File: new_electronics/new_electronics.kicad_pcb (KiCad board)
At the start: 2 copper layers, 17 parts

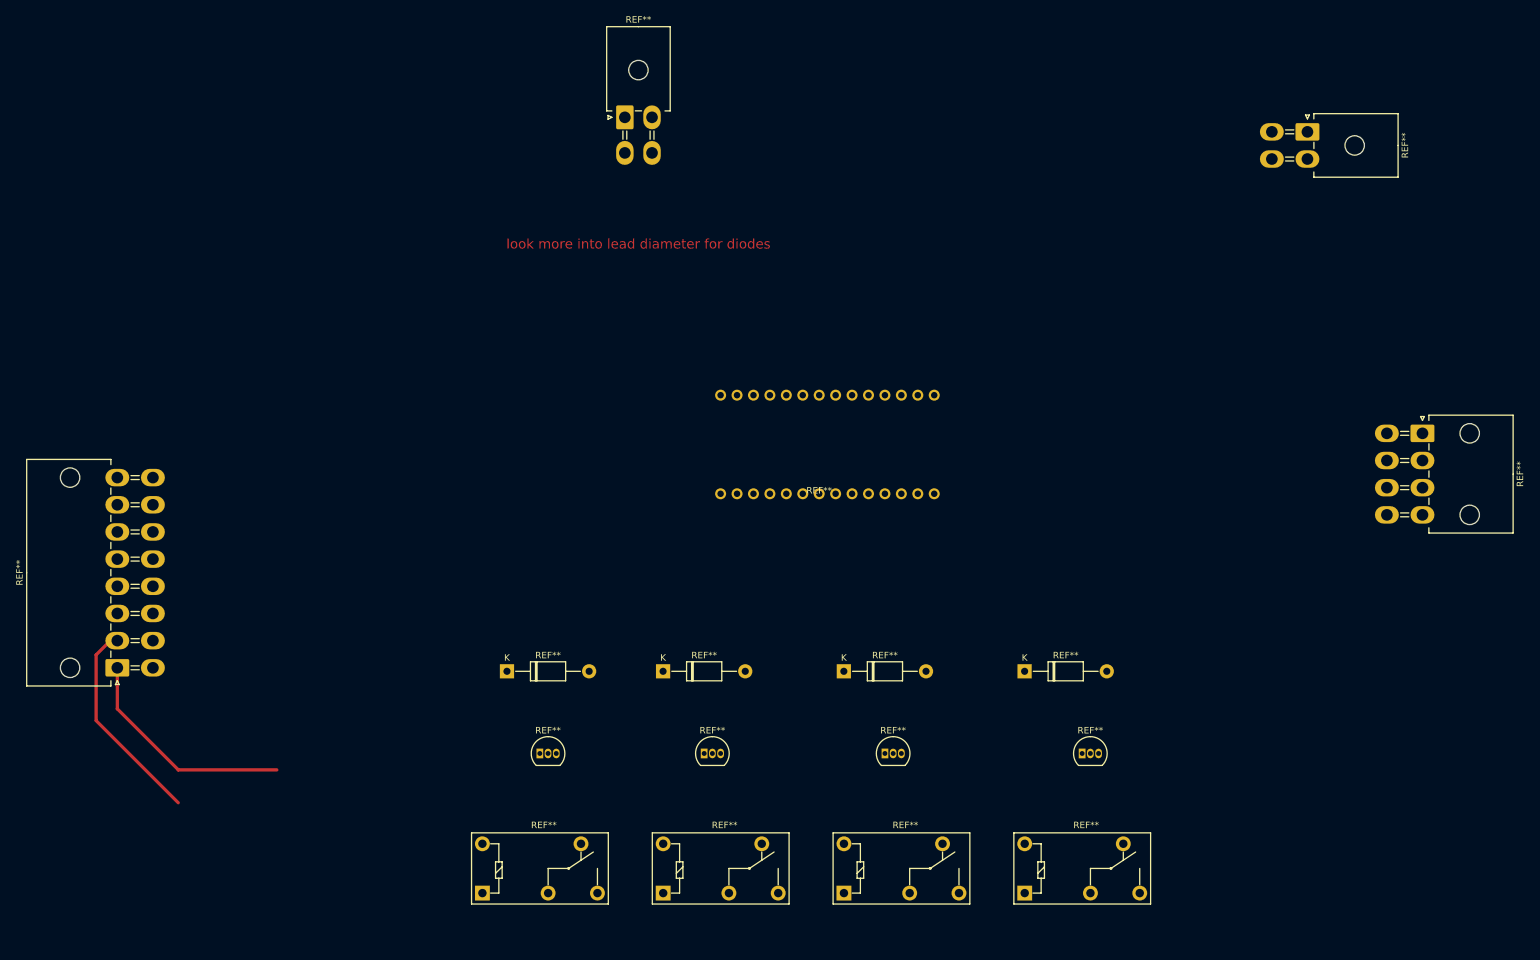
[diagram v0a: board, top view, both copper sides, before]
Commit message: some basic wiring for new pcb
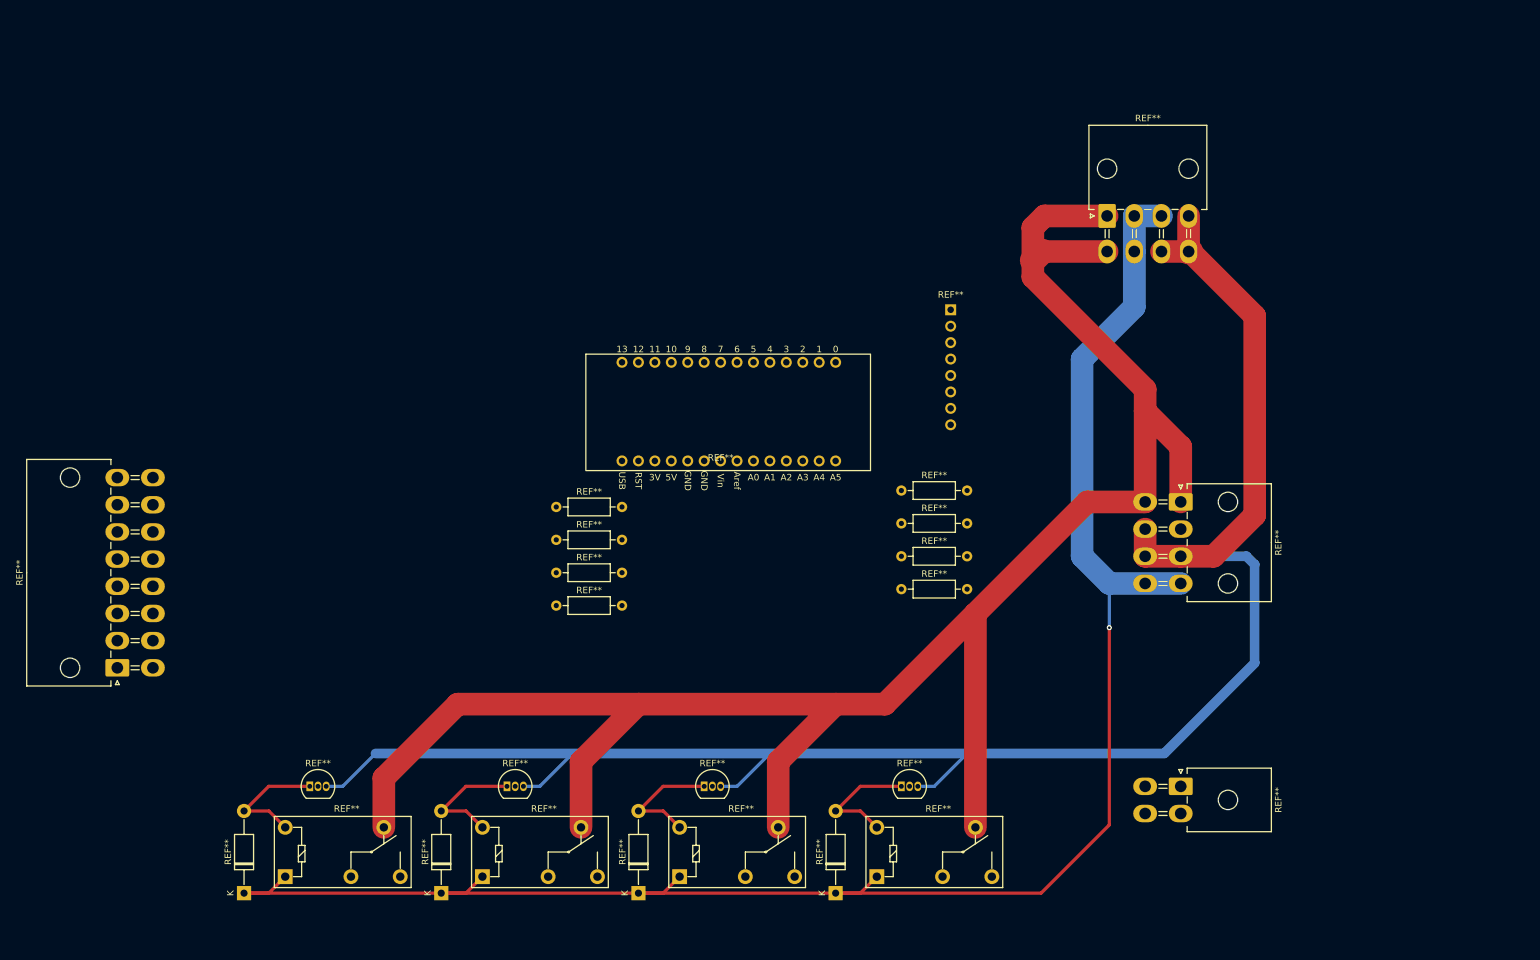
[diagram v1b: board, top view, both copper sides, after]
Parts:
- removed the REF** at (118.1, 119.4)
- removed the REF** at (146.1, 119.4)
- removed the REF** at (112.2, 33.8)
- removed the REF** at (174.0, 119.4)
- added REF**: R_Axial_DIN0207_L6.3mm_D2.5mm_P10.16mm_Horizontal, Resistor_THT:R_Axial_DIN0207_L6.3mm_D2.5mm_P10.16mm_Horizontal, F.Cu at (101.6, 104.1)
- added REF**: R_Axial_DIN0207_L6.3mm_D2.5mm_P10.16mm_Horizontal, Resistor_THT:R_Axial_DIN0207_L6.3mm_D2.5mm_P10.16mm_Horizontal, F.Cu at (101.6, 109.2)
- added REF**: R_Axial_DIN0207_L6.3mm_D2.5mm_P10.16mm_Horizontal, Resistor_THT:R_Axial_DIN0207_L6.3mm_D2.5mm_P10.16mm_Horizontal, F.Cu at (101.6, 94.0)
- added REF**: Molex_Mini-Fit_Jr_5569-08A2_2x04_P4.20mm_Horizontal, Connector_Molex:Molex_Mini-Fit_Jr_5569-08A2_2x04_P4.20mm_Horizontal, F.Cu at (186.7, 49.0)
- added REF**: D_DO-41_SOD81_P12.70mm_Horizontal, Diode_THT:D_DO-41_SOD81_P12.70mm_Horizontal, F.Cu at (114.3, 153.7)
- added REF**: R_Axial_DIN0207_L6.3mm_D2.5mm_P10.16mm_Horizontal, Resistor_THT:R_Axial_DIN0207_L6.3mm_D2.5mm_P10.16mm_Horizontal, F.Cu at (154.9, 101.6)
- added REF**: R_Axial_DIN0207_L6.3mm_D2.5mm_P10.16mm_Horizontal, Resistor_THT:R_Axial_DIN0207_L6.3mm_D2.5mm_P10.16mm_Horizontal, F.Cu at (154.9, 96.5)
- added REF**: D_DO-41_SOD81_P12.70mm_Horizontal, Diode_THT:D_DO-41_SOD81_P12.70mm_Horizontal, F.Cu at (144.8, 153.7)
- added REF**: mpu6050, custom_footprints:mpu6050, F.Cu at (162.6, 71.1)
- added REF**: R_Axial_DIN0207_L6.3mm_D2.5mm_P10.16mm_Horizontal, Resistor_THT:R_Axial_DIN0207_L6.3mm_D2.5mm_P10.16mm_Horizontal, F.Cu at (101.6, 99.1)
- added REF**: R_Axial_DIN0207_L6.3mm_D2.5mm_P10.16mm_Horizontal, Resistor_THT:R_Axial_DIN0207_L6.3mm_D2.5mm_P10.16mm_Horizontal, F.Cu at (154.9, 91.4)
- added REF**: D_DO-41_SOD81_P12.70mm_Horizontal, Diode_THT:D_DO-41_SOD81_P12.70mm_Horizontal, F.Cu at (83.8, 153.7)
- added REF**: R_Axial_DIN0207_L6.3mm_D2.5mm_P10.16mm_Horizontal, Resistor_THT:R_Axial_DIN0207_L6.3mm_D2.5mm_P10.16mm_Horizontal, F.Cu at (154.9, 106.7)
- moved REF** 103.0 mm to (198.1, 137.2)
- moved REF** 53.2 mm to (53.3, 153.7), turned to 90 degrees
- moved REF** 38.8 mm to (198.1, 93.2)
- moved REF** 35.9 mm to (63.5, 137.2)
- moved REF** 30.9 mm to (94.0, 137.2)
- moved REF** 30.6 mm to (59.7, 151.1)
- moved REF** 28.4 mm to (124.5, 137.2)
- moved REF** 28.4 mm to (154.9, 137.2)
- moved REF** 28.1 mm to (90.2, 151.1)
- moved REF** 25.5 mm to (120.7, 151.1)
- moved REF** 23.0 mm to (151.1, 151.1)
- moved REF** 16.1 mm to (127.0, 78.7)
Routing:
- net (no net): track 67.2 -> 957.9 mm, vias 0 -> 1
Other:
- board text removed: "look more into lead diameter for diodes"

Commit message: more new pcb work
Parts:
- removed the REF** at (154.9, 101.6)
- removed the REF** at (154.9, 96.5)
- removed the REF** at (154.9, 91.4)
- removed the REF** at (154.9, 106.7)
- added Controller Vin: TestPoint_Plated_Hole_D2.0mm, TestPoint:TestPoint_Plated_Hole_D2.0mm, F.Cu at (106.7, 87.6)
- added R1: R_Axial_DIN0207_L6.3mm_D2.5mm_P10.16mm_Horizontal, Resistor_THT:R_Axial_DIN0207_L6.3mm_D2.5mm_P10.16mm_Horizontal, F.Cu at (154.3, 78.1)
- added R2: R_Axial_DIN0207_L6.3mm_D2.5mm_P10.16mm_Horizontal, Resistor_THT:R_Axial_DIN0207_L6.3mm_D2.5mm_P10.16mm_Horizontal, F.Cu at (151.1, 78.1)
- added R3: R_Axial_DIN0207_L6.3mm_D2.5mm_P10.16mm_Horizontal, Resistor_THT:R_Axial_DIN0207_L6.3mm_D2.5mm_P10.16mm_Horizontal, F.Cu at (148.0, 78.1)
- added R4: R_Axial_DIN0207_L6.3mm_D2.5mm_P10.16mm_Horizontal, Resistor_THT:R_Axial_DIN0207_L6.3mm_D2.5mm_P10.16mm_Horizontal, F.Cu at (144.8, 78.1)
- added REF**: PinHeader_1x01_P2.54mm_Vertical, Connector_PinHeader_2.54mm:PinHeader_1x01_P2.54mm_Vertical, F.Cu at (125.7, 103.5)
- added REF**: PinHeader_1x03_P2.54mm_Vertical, Connector_PinHeader_2.54mm:PinHeader_1x03_P2.54mm_Vertical, F.Cu at (139.1, 105.4)
- 12-6V Converter: renamed from REF**
- Depth Sensor: renamed from REF**
- Main Connector: renamed from REF**
- Power I/O: renamed from REF**
- moved Main Connector 31.0 mm to (64.1, 125.1)
- moved U2 29.8 mm to (181.6, 94.0)
- moved 12-6V Converter 28.5 mm to (196.9, 75.7)
- moved R5 24.3 mm to (78.7, 85.7), turned to 90 degrees
- moved R6 22.8 mm to (81.9, 87.6), turned to 90 degrees
- moved R8 22.2 mm to (88.3, 91.4), turned to 90 degrees
- moved R7 22.0 mm to (85.1, 89.5), turned to 90 degrees
- moved Power I/O 15.9 mm to (198.1, 109.1)
- moved U1 15.4 mm to (136.5, 90.8)
- renumbered REF** to D1, REF** to D2, REF** to D3, REF** to D4, REF** to K1, REF** to K2, REF** to K3, REF** to K4, REF** to Q1, REF** to Q2, REF** to Q3, REF** to Q4, REF** to R5, REF** to R6, REF** to R7, REF** to R8, REF** to U1, REF** to U2
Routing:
- net (no net): track 957.9 -> 3714.9 mm, vias 1 -> 19
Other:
- board outline added: 165.1 x 101.6 mm

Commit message: 'finished' new pcb
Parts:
- removed Controller Vin: TestPoint_Plated_Hole_D2.0mm, TestPoint:TestPoint_Plated_Hole_D2.0mm
- removed REF**: PinHeader_1x01_P2.54mm_Vertical, Connector_PinHeader_2.54mm:PinHeader_1x01_P2.54mm_Vertical
- removed REF**: PinHeader_1x03_P2.54mm_Vertical, Connector_PinHeader_2.54mm:PinHeader_1x03_P2.54mm_Vertical
- added 8: PinHeader_1x01_P2.54mm_Vertical, Connector_PinHeader_2.54mm:PinHeader_1x01_P2.54mm_Vertical, F.Cu at (67.6, 88.9)
- added Controller Battery: Molex_Mini-Fit_Jr_5569-04A2_2x02_P4.20mm_Horizontal, Connector_Molex:Molex_Mini-Fit_Jr_5569-04A2_2x02_P4.20mm_Horizontal, F.Cu at (169.3, 75.7)
- added D5: LED_D5.0mm, LED_THT:LED_D5.0mm, F.Cu at (55.8, 68.1)
- added D6: LED_D5.0mm, LED_THT:LED_D5.0mm, F.Cu at (65.8, 68.1)
- added D7: LED_D5.0mm, LED_THT:LED_D5.0mm, F.Cu at (75.8, 68.1)
- added J1: PinHeader_1x03_P2.54mm_Vertical, Connector_PinHeader_2.54mm:PinHeader_1x03_P2.54mm_Vertical, F.Cu at (112.8, 107.4)
- added NC: PinHeader_1x01_P2.54mm_Vertical, Connector_PinHeader_2.54mm:PinHeader_1x01_P2.54mm_Vertical, F.Cu at (105.4, 138.5)
- added NC: PinHeader_1x01_P2.54mm_Vertical, Connector_PinHeader_2.54mm:PinHeader_1x01_P2.54mm_Vertical, F.Cu at (135.9, 138.5)
- added NC: PinHeader_1x01_P2.54mm_Vertical, Connector_PinHeader_2.54mm:PinHeader_1x01_P2.54mm_Vertical, F.Cu at (74.9, 138.5)
- added NC: PinHeader_1x01_P2.54mm_Vertical, Connector_PinHeader_2.54mm:PinHeader_1x01_P2.54mm_Vertical, F.Cu at (166.4, 138.5)
- added Q5: TO-92_Inline, Package_TO_SOT_THT:TO-92_Inline, F.Cu at (103.8, 66.0)
- added Q6: TO-92_Inline, Package_TO_SOT_THT:TO-92_Inline, F.Cu at (111.4, 66.0)
- added Q7: TO-92_Inline, Package_TO_SOT_THT:TO-92_Inline, F.Cu at (119.0, 66.0)
- added Q8: TO-92_Inline, Package_TO_SOT_THT:TO-92_Inline, F.Cu at (173.9, 123.7)
- added R10: R_Axial_DIN0207_L6.3mm_D2.5mm_P15.24mm_Horizontal, Resistor_THT:R_Axial_DIN0207_L6.3mm_D2.5mm_P15.24mm_Horizontal, F.Cu at (112.6, 73.4)
- added R11: R_Axial_DIN0207_L6.3mm_D2.5mm_P10.16mm_Horizontal, Resistor_THT:R_Axial_DIN0207_L6.3mm_D2.5mm_P10.16mm_Horizontal, F.Cu at (121.3, 80.8)
- added R12: R_Axial_DIN0207_L6.3mm_D2.5mm_P10.16mm_Horizontal, Resistor_THT:R_Axial_DIN0207_L6.3mm_D2.5mm_P10.16mm_Horizontal, F.Cu at (138.2, 66.5)
- added R13: R_Axial_DIN0207_L6.3mm_D2.5mm_P10.16mm_Horizontal, Resistor_THT:R_Axial_DIN0207_L6.3mm_D2.5mm_P10.16mm_Horizontal, F.Cu at (138.2, 69.6)
- added R14: R_Axial_DIN0207_L6.3mm_D2.5mm_P10.16mm_Horizontal, Resistor_THT:R_Axial_DIN0207_L6.3mm_D2.5mm_P10.16mm_Horizontal, F.Cu at (138.2, 72.6)
- added R15: R_Axial_DIN0207_L6.3mm_D2.5mm_P10.16mm_Horizontal, Resistor_THT:R_Axial_DIN0207_L6.3mm_D2.5mm_P10.16mm_Horizontal, F.Cu at (190.0, 127.8)
- added R16: R_Axial_DIN0207_L6.3mm_D2.5mm_P10.16mm_Horizontal, Resistor_THT:R_Axial_DIN0207_L6.3mm_D2.5mm_P10.16mm_Horizontal, F.Cu at (169.9, 116.3)
- added R9: R_Axial_DIN0207_L6.3mm_D2.5mm_P15.24mm_Horizontal, Resistor_THT:R_Axial_DIN0207_L6.3mm_D2.5mm_P15.24mm_Horizontal, F.Cu at (109.5, 73.4)
- moved R5 13.0 mm to (91.7, 85.7)
- moved R6 13.0 mm to (94.9, 87.6)
- moved R7 13.0 mm to (98.0, 89.5)
- moved R8 13.0 mm to (101.2, 91.4)
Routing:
- net (no net): track 3714.9 -> 4414.5 mm, vias 19 -> 21
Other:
- board size 165.1 x 101.6 mm -> 164.3 x 101.6 mm
- board text added: "+12V"
- board text added: "+5V"
- board text added: "+6V"
- board text added: "1"
- board text added: "10"
- board text added: "11"
- board text added: "12"
- board text added: "13"
- board text added: "14"
- board text added: "15"
- board text added: "16"
- board text added: "2"
- board text added: "3"
- board text added: "4"
- board text added: "5"
- board text added: "6"
- board text added: "7"
- board text added: "8"
- board text added: "9"
- board text added: "Button/Switch Pulldown Resistors"
- board text added: "C B E"
- board text added: "External LED"
- board text added: "GND"
- board text added: "LED Resistors"
- board text added: "LED Transistor Resistors"
- board text added: "MPU6050"
- board text added: "Relay Transistor Resistors"
- board text added: "SCL"
- board text added: "SDA"
- board text added: "Status LEDs"
- board text added: "Vbat"

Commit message: small changes still to new pcb
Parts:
- moved Main Connector 0.64 mm to (63.5, 125.1)
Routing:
- net (no net): track 4414.5 -> 4416.7 mm
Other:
- board size 164.3 x 101.6 mm -> 165.1 x 101.6 mm
